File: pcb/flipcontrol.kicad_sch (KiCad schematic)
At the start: 43 parts, among them J1 PJ-202A, J2 DOT_BOARD_1, J3 LED_STRIP, Q1 UMH3N, Q2 FQP27P06, Q3 2N3904BU, Q4 FQP27P06, Q5 2N3904BU, U1 LM2576HVT-5, U2 LM1085-3.3, U3 CH340C, U3 ESP32-S3-WROOM-1

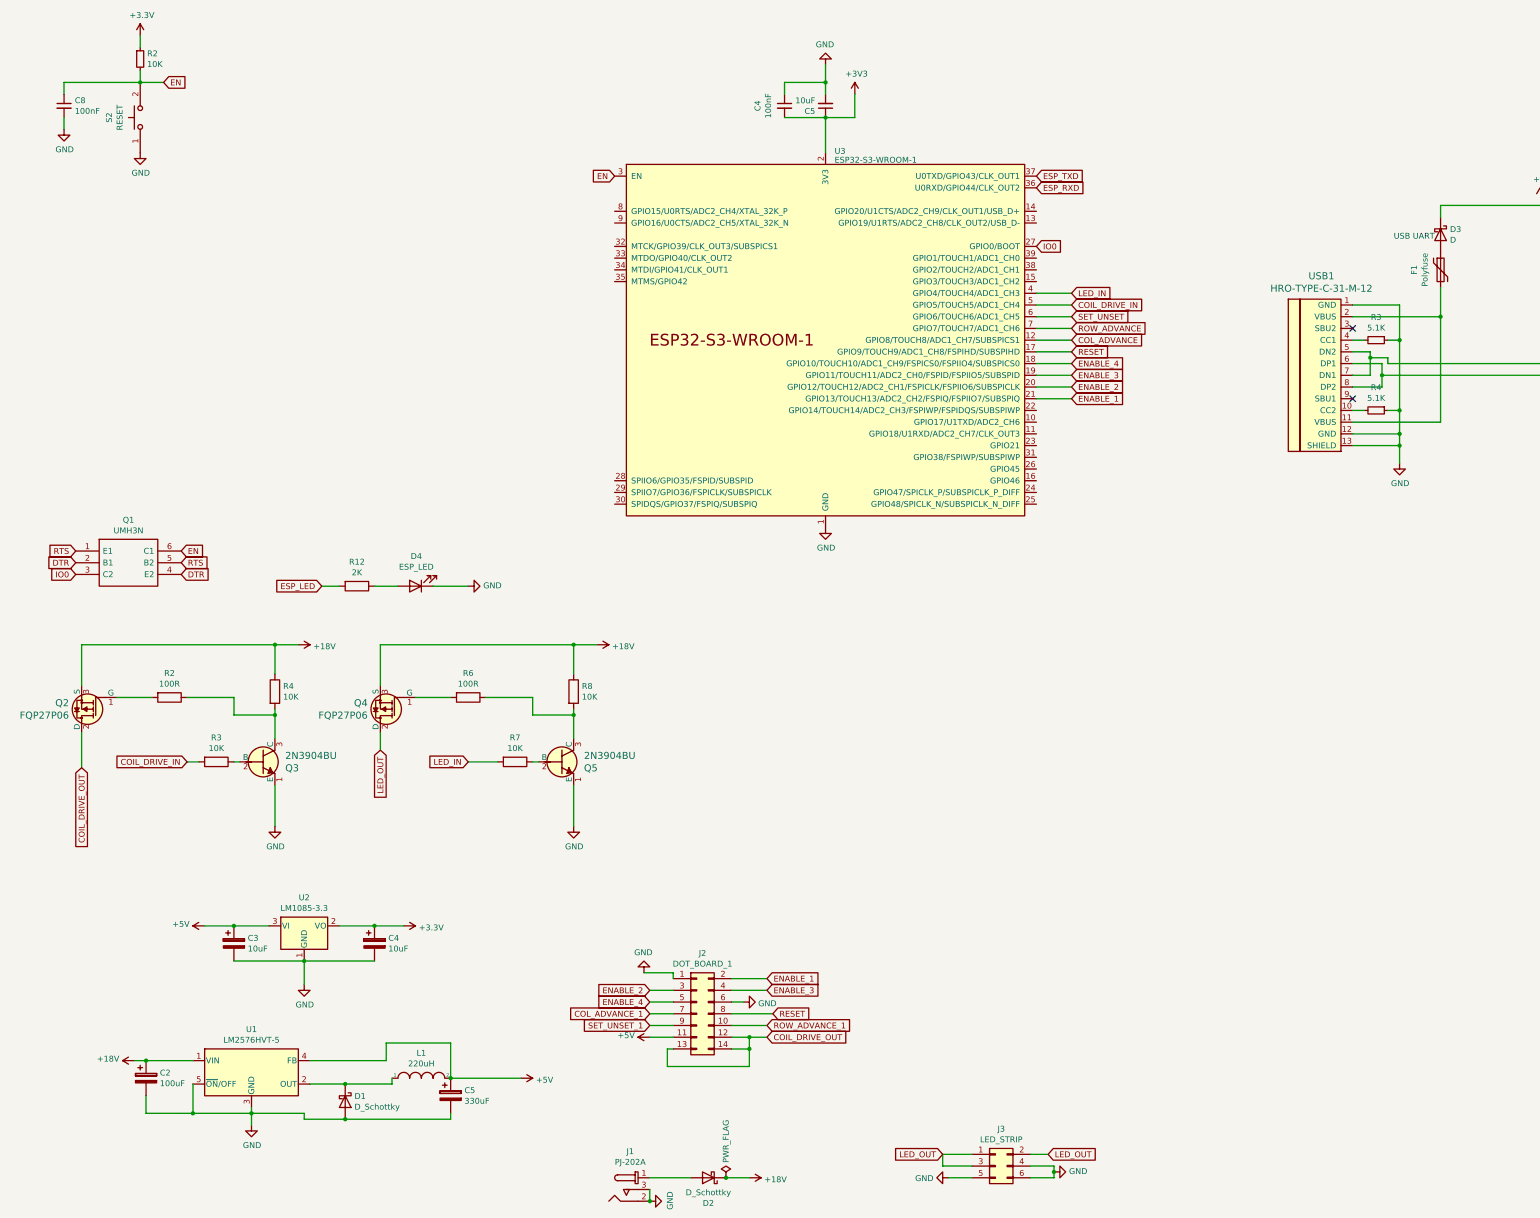
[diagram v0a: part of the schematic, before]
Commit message: Update schematic with newer parts
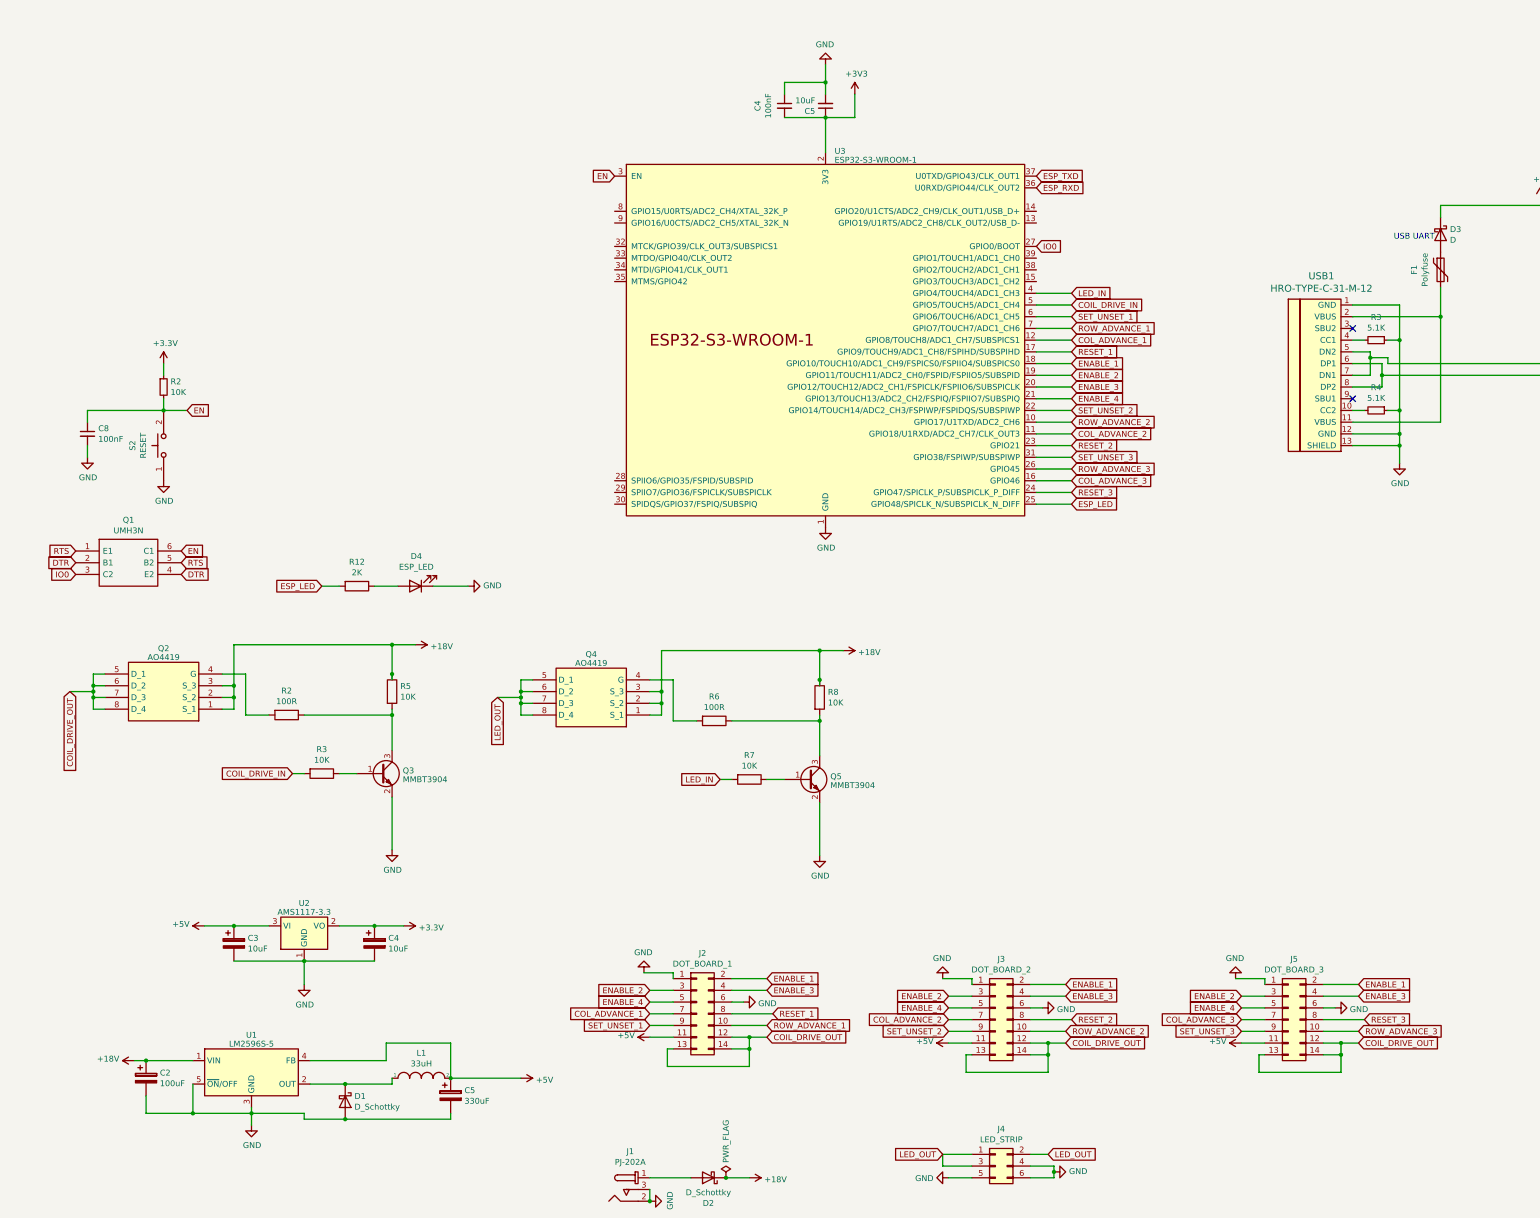
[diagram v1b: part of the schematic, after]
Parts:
- removed Q2, Q4: FQP27P06, digikey-footprints:TO-220-3, symbol flipcontrol-rescue:FQP27P06-dk_Transistors-FETs-MOSFETs-Single
- removed Q3, Q5: 2N3904BU, digikey-footprints:TO-92-3, symbol flipcontrol-rescue:2N3904BU-dk_Transistors-Bipolar-BJT-Single
- removed U1: LM2576HVT-5, Package_TO_SOT_SMD:TO-263-5_TabPin3, symbol Regulator_Switching:LM2576HVT-5
- removed U2: LM1085-3.3, Package_TO_SOT_SMD:TO-263-3_TabPin2, symbol Regulator_Linear:LM1085-3.3
- added J3: DOT_BOARD_2, Connector_IDC:IDC-Header_2x07_P2.54mm_Vertical, symbol Connector_Generic:Conn_02x07_Odd_Even
- added J5: DOT_BOARD_3, Connector_IDC:IDC-Header_2x07_P2.54mm_Vertical, symbol Connector_Generic:Conn_02x07_Odd_Even
- added Q2, Q4: AO4419, SOIC127P600X175-8N, symbol SamacSys_Parts:AO4419
- added Q3, Q5: MMBT3904, Package_TO_SOT_SMD:SOT-23, symbol Transistor_BJT:MMBT3904
- added U1: LM2596S-5, Package_TO_SOT_SMD:TO-263-5_TabPin3, symbol Regulator_Switching:LM2596S-5
- added U2: AMS1117-3.3, Package_TO_SOT_SMD:SOT-223-3_TabPin2, symbol Regulator_Linear:AMS1117-3.3
- L1: value 220uH -> 33uH
- renumbered J3 to J4, R4 to R5
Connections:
- net COL_ADVANCE is gone; now on net COL_ADVANCE_1: U3.12 (GPIO8/TOUCH8/ADC1_CH7/SUBSPICS1)
- net ROW_ADVANCE is gone; now on net ROW_ADVANCE_1: U3.7 (GPIO7/TOUCH7/ADC1_CH6)
- net SET_UNSET is gone; now on net SET_UNSET_1: U3.6 (GPIO6/TOUCH6/ADC1_CH5)
- net +24V: now also Q2.1 (S_1), Q2.2 (S_2), Q2.3 (S_3), Q4.1 (S_1), Q4.2 (S_2), Q4.3 (S_3), U1.1 (VIN)
- net +3V3: now also U2.2 (VO)
- net +5V: now also J3.11 (Pin_11), J5.11 (Pin_11), U1.4 (FB), U2.3 (VI)
- net COIL_DRIVE_OUT: now also J3.12 (Pin_12), J3.13 (Pin_13), J3.14 (Pin_14), J5.12 (Pin_12), J5.13 (Pin_13), J5.14 (Pin_14), Q2.5 (D_1), Q2.6 (D_2), Q2.7 (D_3), Q2.8 (D_4)
- net ENABLE_1: now also U3.18 (GPIO10/TOUCH10/ADC1_CH9/FSPICS0/FSPIIO4/SUBSPICS0), J3.2 (Pin_2), J5.2 (Pin_2); no longer U3.21 (GPIO13/TOUCH13/ADC2_CH2/FSPIQ/FSPIIO7/SUBSPIQ)
- net ENABLE_2: now also U3.19 (GPIO11/TOUCH11/ADC2_CH0/FSPID/FSPIIO5/SUBSPID), J3.3 (Pin_3), J5.3 (Pin_3); no longer U3.20 (GPIO12/TOUCH12/ADC2_CH1/FSPICLK/FSPIIO6/SUBSPICLK)
- net ENABLE_3: now also U3.20 (GPIO12/TOUCH12/ADC2_CH1/FSPICLK/FSPIIO6/SUBSPICLK), J3.4 (Pin_4), J5.4 (Pin_4); no longer U3.19 (GPIO11/TOUCH11/ADC2_CH0/FSPID/FSPIIO5/SUBSPID)
- net ENABLE_4: now also U3.21 (GPIO13/TOUCH13/ADC2_CH2/FSPIQ/FSPIIO7/SUBSPIQ), J3.5 (Pin_5), J5.5 (Pin_5); no longer U3.18 (GPIO10/TOUCH10/ADC1_CH9/FSPICS0/FSPIIO4/SUBSPICS0)
- net ESP_LED: now also U3.25 (GPIO48/SPICLK_N/SUBSPICLK_N_DIFF)
- net GND: now also J3.1 (Pin_1), J3.6 (Pin_6), J5.1 (Pin_1), J5.6 (Pin_6), Q3.2 (E), Q5.2 (E), U1.3 (GND), U1.5 (~{ON}/OFF), U2.1 (GND)
- net LED_OUT: now also Q4.5 (D_1), Q4.6 (D_2), Q4.7 (D_3), Q4.8 (D_4)
- net at D1.1 (K), L1.1: now also U1.2 (OUT)
- net at R3.1: now also Q3.1 (B)
- net at R2.1, R5.2: now also Q3.3 (C)
- net at R2.2: now also Q2.4 (G)
- net at R6.2: now also Q4.4 (G)
- net at R7.1: now also Q5.1 (B)
- net at R6.1, R8.2: now also Q5.3 (C)
- net ROW_ADVANCE_2: now reaches U3.10 (GPIO17/U1TXD/ADC2_CH6)
- net ROW_ADVANCE_2: now also J3.10 (Pin_10)
- net COL_ADVANCE_2: now reaches U3.11 (GPIO18/U1RXD/ADC2_CH7/CLK_OUT3)
- net COL_ADVANCE_2: now also J3.7 (Pin_7)
- net COL_ADVANCE_3: now reaches U3.16 (GPIO46)
- net COL_ADVANCE_3: now also J5.7 (Pin_7)
- net SET_UNSET_2: now reaches U3.22 (GPIO14/TOUCH14/ADC2_CH3/FSPIWP/FSPIDQS/SUBSPIWP)
- net SET_UNSET_2: now also J3.9 (Pin_9)
- net RESET_2: now reaches U3.23 (GPIO21)
- net RESET_2: now also J3.8 (Pin_8)
- net RESET_3: now reaches U3.24 (GPIO47/SPICLK_P/SUBSPICLK_P_DIFF)
- net RESET_3: now also J5.8 (Pin_8)
- net ROW_ADVANCE_3: now reaches U3.26 (GPIO45)
- net ROW_ADVANCE_3: now also J5.10 (Pin_10)
- net SET_UNSET_3: now reaches U3.31 (GPIO38/FSPIWP/SUBSPIWP)
- net SET_UNSET_3: now also J5.9 (Pin_9)
- net RESET renamed RESET_1
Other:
- moved on the sheet: C8, R2, R3, R5, S2

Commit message: Update PCB
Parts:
- C2: footprint Capacitor_THT:CP_Radial_D5.0mm_P2.50mm -> Capacitor_SMD:CP_Elec_10x10
- C3, C4: footprint Capacitor_THT:CP_Radial_D5.0mm_P2.50mm -> Capacitor_SMD:C_0805_2012Metric
- C5: value 330uF -> 220uF; footprint Capacitor_THT:CP_Radial_D5.0mm_P2.50mm -> Capacitor_SMD:CP_Elec_10x10
- D1: footprint Diode_THT:D_DO-15_P10.16mm_Horizontal -> Diode_SMD:D_SMB
- D2: value D_Schottky -> D
- L1: footprint Inductor_THT:L_Radial_D8.7mm_P5.00mm_Fastron_07HCP -> Inductor_SMD:L_12x12mm_H6mm; Part (none) -> SMDRI127-330MT
- Q2, Q4: footprint SOIC127P600X175-8N -> SamacSys_Parts:SOIC127P600X175-8N
- R2, R3, R5, R6, R7, R8: footprint Resistor_THT:R_Axial_DIN0204_L3.6mm_D1.6mm_P5.08mm_Horizontal -> Resistor_SMD:R_0805_2012Metric
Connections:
- no-connect marks 2 -> 21
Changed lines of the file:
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@@
 (kicad_sch (version 20230121) (generator eeschema)
   (paper "A3")
+  (junction (at 93.98 152.4) (diameter 0) (color 0 0 0 0)
+  )
   (junction (at 186.69 168.91) (diameter 0) (color 0 0 0 0)
   )
@@
   (junction (at 312.42 106.68) (diameter 0) (color 0 0 0 0)
   )
-  (junction (at 186.69 153.67) (diameter 0) (color 0 0 0 0)
-  )
   (junction (at 237.49 266.7) (diameter 0) (color 0 0 0 0)
   )
@@
   (junction (at 367.03 31.75) (diameter 0) (color 0 0 0 0)
   )
-  (junction (at 93.98 158.75) (diameter 0) (color 0 0 0 0)
-  )
   (junction (at 152.4 165.1) (diameter 0) (color 0 0 0 0)
   )
   (junction (at 370.84 31.75) (diameter 0) (color 0 0 0 0)
   )
-  (junction (at 93.98 152.4) (diameter 0) (color 0 0 0 0)
-  )
   (junction (at 171.45 237.49) (diameter 0) (color 0 0 0 0)
   )
@@
   (junction (at 83.82 255.27) (diameter 0) (color 0 0 0 0)
   )
+  (junction (at 186.69 153.67) (diameter 0) (color 0 0 0 0)
+  )
   (junction (at 299.72 238.76) (diameter 0) (color 0 0 0 0)
   )
@@
   (junction (at 63.5 254) (diameter 0) (color 0 0 0 0)
   )
-  (junction (at 186.69 160.02) (diameter 0) (color 0 0 0 0)
-  )
   (junction (at 59.69 161.29) (diameter 0) (color 0 0 0 0)
   )
@@
   (junction (at 187.96 38.1) (diameter 0) (color 0 0 0 0)
   )
+  (no_connect (at 374.65 93.98))
+  (no_connect (at 142.24 68.58))
+  (no_connect (at 142.24 73.66))
+  (no_connect (at 142.24 60.96))
   (no_connect (at 302.26 99.06))
+  (no_connect (at 142.24 121.92))
+  (no_connect (at 233.68 73.66))
+  (no_connect (at 142.24 119.38))
+  (no_connect (at 142.24 116.84))
+  (no_connect (at 142.24 58.42))
+  (no_connect (at 374.65 91.44))
+  (no_connect (at 233.68 58.42))
+  (no_connect (at 142.24 71.12))
+  (no_connect (at 142.24 66.04))
+  (no_connect (at 374.65 88.9))
+  (no_connect (at 374.65 96.52))
+  (no_connect (at 233.68 60.96))
+  (no_connect (at 354.33 83.82))
+  (no_connect (at 233.68 71.12))
+  (no_connect (at 233.68 68.58))
   (no_connect (at 302.26 83.82))
   (wire (pts (xy 378.46 46.99) (xy 372.11 46.99))
@@
     (stroke (width 0) (type default))
   )
+  (wire (pts (xy 186.69 153.67) (xy 186.69 160.02))
+    (stroke (width 0) (type default))
+  )
   (wire (pts (xy 49.53 101.6) (xy 44.45 101.6))
     (stroke (width 0) (type default))
@@
     (stroke (width 0) (type default))
   )
-  (wire (pts (xy 152.4 153.67) (xy 186.69 153.67))
-    (stroke (width 0) (type default))
-  )
   (wire (pts (xy 232.41 267.97) (xy 237.49 267.97))
     (stroke (width 0) (type default))
@@
     (stroke (width 0) (type default))
   )
-  (wire (pts (xy 186.69 161.29) (xy 186.69 160.02))
-    (stroke (width 0) (type default))
-  )
   (wire (pts (xy 312.42 109.22) (xy 312.42 113.03))
     (stroke (width 0) (type default))
@@
     (stroke (width 0) (type default))
   )
-  (wire (pts (xy 186.69 153.67) (xy 186.69 160.02))
-    (stroke (width 0) (type default))
-  )
   (wire (pts (xy 278.13 231.14) (xy 283.21 231.14))
     (stroke (width 0) (type default))
@@
     (stroke (width 0) (type default))
   )
-  (wire (pts (xy 93.98 160.02) (xy 93.98 158.75))
-    (stroke (width 0) (type default))
-  )
   (wire (pts (xy 236.22 241.3) (xy 232.41 241.3))
     (stroke (width 0) (type default))
@@
     (stroke (width 0) (type default))
   )
-  (wire (pts (xy 186.69 153.67) (xy 191.77 153.67))
+  (wire (pts (xy 152.4 153.67) (xy 186.69 153.67))
     (stroke (width 0) (type default))
   )
@@
     (stroke (width 0) (type default))
   )
-  (wire (pts (xy 93.98 152.4) (xy 99.06 152.4))
-    (stroke (width 0) (type default))
-  )
   (wire (pts (xy 83.82 255.27) (xy 106.68 255.27))
     (stroke (width 0) (type default))
@@
     (stroke (width 0) (type default))
   )
+  (wire (pts (xy 93.98 152.4) (xy 99.06 152.4))
+    (stroke (width 0) (type default))
+  )
   (wire (pts (xy 121.92 165.1) (xy 121.92 167.64))
     (stroke (width 0) (type default))
@@
     (stroke (width 0) (type default))
   )
+  (wire (pts (xy 93.98 152.4) (xy 93.98 158.75))
+    (stroke (width 0) (type default))
+  )
   (wire (pts (xy 72.39 180.34) (xy 74.93 180.34))
     (stroke (width 0) (type default))
@@
     (stroke (width 0) (type default))
   )
-  (wire (pts (xy 93.98 152.4) (xy 93.98 158.75))
-    (stroke (width 0) (type default))
-  )
   (wire (pts (xy 121.92 167.64) (xy 124.46 167.64))
     (stroke (width 0) (type default))
@@
     (stroke (width 0) (type default))
   )
+  (wire (pts (xy 186.69 153.67) (xy 191.77 153.67))
+    (stroke (width 0) (type default))
+  )
   (wire (pts (xy 149.86 237.49) (xy 154.94 237.49))
     (stroke (width 0) (type default))
@@
       (effects (font (size 1.27 1.27)))
     )
-    (property "Footprint" "Inductor_THT:L_Radial_D8.7mm_P5.00mm_Fastron_07HCP" (at 100.33 246.38 0)
+    (property "Footprint" "Inductor_SMD:L_12x12mm_H6mm" (at 100.33 246.38 0)
       (effects (font (size 1.27 1.27)) hide)
     )
@@
       (effects (font (size 1.27 1.27)) hide)
     )
+    (property "Part" "SMDRI127-330MT" (at 100.33 246.38 0)
+      (effects (font (size 1.27 1.27)) hide)
+    )
+    (property "Field5" "" (at 100.33 246.38 0)
+      (effects (font (size 1.27 1.27)) hide)
+    )
     (pin "1")
     (pin "2")
@@
       (effects (font (size 1.27 1.27)) (justify left))
     )
-    (property "Footprint" "Diode_THT:D_DO-15_P10.16mm_Horizontal" (at 83.82 251.46 0)
+    (property "Footprint" "Diode_SMD:D_SMB" (at 83.82 251.46 0)
       (effects (font (size 1.27 1.27)) hide)
     )
@@
       (effects (font (size 1.27 1.27)) (justify left))
     )
-    (property "Value" "330uF" (at 109.6772 251.333 0)
+    (property "Value" "220uF" (at 109.6772 251.333 0)
       (effects (font (size 1.27 1.27)) (justify left))
     )
-    (property "Footprint" "Capacitor_THT:CP_Radial_D5.0mm_P2.50mm" (at 107.6452 254 0)
+    (property "Footprint" "Capacitor_SMD:CP_Elec_10x10" (at 107.6452 254 0)
       (effects (font (size 1.27 1.27)) hide)
     )
@@
       (effects (font (size 1.27 1.27)) (justify left))
     )
-    (property "Footprint" "Capacitor_THT:CP_Radial_D5.0mm_P2.50mm" (at 41.6052 250.19 0)
+    (property "Footprint" "Capacitor_SMD:CP_Elec_10x10" (at 41.6052 250.19 0)
       (effects (font (size 1.27 1.27)) hide)
     )
@@
       (effects (font (size 1.27 1.27)) (justify left))
     )
-    (property "Footprint" "Capacitor_THT:CP_Radial_D5.0mm_P2.50mm" (at 60.6552 220.98 0)
+    (property "Footprint" "Capacitor_SMD:C_0805_2012Metric" (at 60.6552 220.98 0)
       (effects (font (size 1.27 1.27)) hide)
     )
@@
       (effects (font (size 1.27 1.27)) (justify left))
     )
-    (property "Footprint" "Capacitor_THT:CP_Radial_D5.0mm_P2.50mm" (at 91.1352 220.98 0)
+    (property "Footprint" "Capacitor_SMD:C_0805_2012Metric" (at 91.1352 220.98 0)
       (effects (font (size 1.27 1.27)) hide)
     )
@@
       (effects (font (size 1.27 1.27)) (justify left))
     )
-    (property "Footprint" "Resistor_THT:R_Axial_DIN0204_L3.6mm_D1.6mm_P5.08mm_Horizontal" (at 92.202 162.56 90)
+    (property "Footprint" "Resistor_SMD:R_0805_2012Metric" (at 92.202 162.56 90)
       (effects (font (size 1.27 1.27)) hide)
     )
@@
       (effects (font (size 1.27 1.27)))
     )
-    (property "Footprint" "Resistor_THT:R_Axial_DIN0204_L3.6mm_D1.6mm_P5.08mm_Horizontal" (at 71.12 165.862 90)
+    (property "Footprint" "Resistor_SMD:R_0805_2012Metric" (at 71.12 165.862 90)
       (effects (font (size 1.27 1.27)) hide)
     )
@@
       (effects (font (size 1.27 1.27)))
     )
-    (property "Footprint" "Resistor_THT:R_Axial_DIN0204_L3.6mm_D1.6mm_P5.08mm_Horizontal" (at 78.74 178.562 90)
+    (property "Footprint" "Resistor_SMD:R_0805_2012Metric" (at 78.74 178.562 90)
       (effects (font (size 1.27 1.27)) hide)
     )
@@
       (effects (font (size 1.27 1.27)) (justify left))
     )
-    (property "Footprint" "Resistor_THT:R_Axial_DIN0204_L3.6mm_D1.6mm_P5.08mm_Horizontal" (at 184.912 163.83 90)
+    (property "Footprint" "Resistor_SMD:R_0805_2012Metric" (at 184.912 163.83 90)
       (effects (font (size 1.27 1.27)) hide)
     )
@@
       (effects (font (size 1.27 1.27)))
     )
-    (property "Footprint" "SOIC127P600X175-8N" (at 128.27 72.72 0)
+    (property "Footprint" "SamacSys_Parts:SOIC127P600X175-8N" (at 128.27 72.72 0)
       (effects (font (size 1.27 1.27)) (justify left top) hide)
     )
@@
       (effects (font (size 1.27 1.27)))
     )
-    (property "Value" "D_Schottky" (at 162.56 271.1704 0)
+    (property "Value" "D" (at 162.56 271.1704 0)
       (effects (font (size 1.27 1.27)))
     )
@@
       (effects (font (size 1.27 1.27)))
     )
-    (property "Footprint" "Resistor_THT:R_Axial_DIN0204_L3.6mm_D1.6mm_P5.08mm_Horizontal" (at 163.83 167.132 90)
+    (property "Footprint" "Resistor_SMD:R_0805_2012Metric" (at 163.83 167.132 90)
       (effects (font (size 1.27 1.27)) hide)
     )
@@
       (effects (font (size 1.27 1.27)))
     )
-    (property "Footprint" "Resistor_THT:R_Axial_DIN0204_L3.6mm_D1.6mm_P5.08mm_Horizontal" (at 171.45 179.832 90)
+    (property "Footprint" "Resistor_SMD:R_0805_2012Metric" (at 171.45 179.832 90)
       (effects (font (size 1.27 1.27)) hide)
     )
@@
       (effects (font (size 1.27 1.27)))
     )
-    (property "Footprint" "SOIC127P600X175-8N" (at 35.56 71.45 0)
+    (property "Footprint" "SamacSys_Parts:SOIC127P600X175-8N" (at 35.56 71.45 0)
       (effects (font (size 1.27 1.27)) (justify left top) hide)
     )

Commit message: Update with latest schematic and board changes
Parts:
- removed Q2, Q4: AO4419, SamacSys_Parts:SOIC127P600X175-8N, symbol SamacSys_Parts:AO4419
- added Q2, Q4: Si2347DS-T1-GE3, SOT95P237X112-3N, symbol SamacSys_Parts:Si2347DS-T1-GE3
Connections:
- net +24V: now also Q2.2 (S), Q4.2 (S)
- net COIL_DRIVE_OUT: now also Q2.3 (D)
- net LED_OUT: now also Q4.3 (D)
- net at R2.2: now also Q2.1 (G)
- net at R6.2: now also Q4.1 (G)
